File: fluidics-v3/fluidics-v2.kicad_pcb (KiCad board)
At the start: 4 copper layers, 85 x 95.5 mm, 82 parts, among them IC2 ADUM1250WSRZ-RL7, J1 PJ-063AH, J10 87832-0410, J11 0705430001, J12 87832-0410, J13 0705430001, J14 87832-0410, J15 0533980671, J16 0705430001, J17 0533980671, J18 87832-0410, J19 0705430001, J2 B6B-ZR-SM4-TF, J20 0533980671, J21 87832-0410, J22 0705430001, J24 0705430001, J25 87832-0410, J3 A-DS_15_A_KG-T4S, J4 B6B-ZR-SM4-TF, J5 Screw_Terminal_01x06, U1 TPL7407LDR, U11 MAX3221, U12 CD4050BDR, U13 TC7PZ17FU, U2 Teensy4.1, U3 AP7366EA-33W5-7, U4 D24V10FX, U6 LTC4311CSC6-TRPBF

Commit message: v3: mounting holes M2->M3, relink C3/C4/C10, regen fab package
Mounting holes H2-H4: MountingHole_2.2mm_M2 -> 3.2mm_M3 (PCB + schematic,
parity clean). Note: still 3 holes, no H1 (the original board had 4x M3).

Fix bulk-cap schematic links. C3/C4/C10 had no (path) link to their
symbols and lacked the library prefix in their footprint id, so "Update
PCB from Schematic" deleted and re-added them (losing routing). Relinked:
- C3  Capacitor_Tantalum_SMD:CP_EIA-7343-20_Kemet-V -> /cbfc97bd
- C4  Capacitor_SMD:C_1206_3216Metric              -> /5064b71f
- C10 Capacitor_SMD:C_1210_3225Metric              -> /25d2ffd2

Regenerated fabrication/v3 (gerbers, drill incl. new 3.2mm tool, gerber
zip, STEP, BOM, positions) to reflect the M3 holes.

DRC: 0 clearance/hole/short/isolated, 0 schematic-parity. Remaining are
pre-existing: 24 malformed_courtyard on U2 (footprint geometry) and 6
unconnected (5 intentional U2 no-connects + 1 +5V stub).

Co-Authored-By: Claude Opus 4.8 (1M context) <noreply@anthropic.com>
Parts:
- C10: footprint C_1210_3225Metric -> Capacitor_SMD:C_1210_3225Metric
- C3: footprint CP_EIA-7343-20_Kemet-V -> Capacitor_Tantalum_SMD:CP_EIA-7343-20_Kemet-V
- C4: footprint C_1206_3216Metric -> Capacitor_SMD:C_1206_3216Metric
- H2, H3, H4: footprint MountingHole:MountingHole_2.2mm_M2_Pad_Via -> MountingHole:MountingHole_3.2mm_M3_Pad_Via
- moved H3 3.30 mm to (188.7, 111.7)
- moved H2 1.04 mm to (114.0, 38.6)
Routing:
- net /Selector Valves/SCL 5V: track 86.3 -> 86.0 mm, vias 2 -> 1

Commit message: v3: align mounting holes to shared X/Y + regen fab
Snap M3 mounting holes onto shared orthogonal lines for manufacturing:
- Left column H2, H4 -> X = 114 (H4 moved 115->114; H2 kept, since X=115
  overlaps C6 courtyard + the +24V zone)
- Bottom row  H4, H3 -> Y = 112 (H3 moved 111.697->112)

Refilled all 8 copper zones so the +24V/+5V planes carve correctly
around the relocated holes. Regenerated fabrication/v3 (gerbers, drill,
gerber zip, STEP, positions) to match.

DRC: 0 clearance/hole/courtyard/short/isolated, 0 schematic-parity.
Remaining pre-existing: 24 malformed_courtyard on U2, 6 unconnected
(5 intentional U2 no-connects + 1 +5V stub).

Co-Authored-By: Claude Opus 4.8 (1M context) <noreply@anthropic.com>
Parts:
- moved H4 1.00 mm to (114.0, 112.0)
- moved H3 0.30 mm to (188.7, 112.0)
- turned H2 to 90 degrees
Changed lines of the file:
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@@
 	(footprint "MountingHole:MountingHole_3.2mm_M3_Pad_Via"
 		(layer "F.Cu")
-		(at 114 38.631)
+		(at 114 38.631 90)
 		(descr "Mounting Hole 3.2mm, M3, generated by kicad-footprint-generator mountinghole.py")
 		(tags "mountinghole M3")
 		(property "Reference" "H2"
-			(at 0 -4.15 0)
+			(at 0 -4.15 90)
 			(layer "F.SilkS")
 			(effects
@@
 		)
 		(property "Value" "MountingHole_Pad"
-			(at 0 4.15 0)
+			(at 0 4.15 90)
 			(layer "F.Fab")
 			(effects
@@
 		)
 		(property "Datasheet" ""
-			(at 0 0 0)
+			(at 0 0 90)
 			(layer "F.Fab")
 			(hide yes)
@@
 		)
 		(property "Description" ""
-			(at 0 0 0)
+			(at 0 0 90)
 			(layer "F.Fab")
 			(hide yes)
@@
 		)
 		(property "KiLib_Generator" "mounting_hardware/mounting_hole"
-			(at 0 0 0)
+			(at 0 0 90)
 			(layer "F.SilkS")
 			(hide yes)
@@
 		)
 		(fp_text user "${REFERENCE}"
-			(at 0 0 0)
+			(at 0 0 90)
 			(layer "F.Fab")
 			(effects
@@
 		)
 		(pad "1" thru_hole circle
-			(at -2.4 0)
+			(at -2.4 0 90)
 			(size 0.8 0.8)
 			(drill 0.5)
@@
 		)
 		(pad "1" thru_hole circle
-			(at -1.697056 -1.697056)
+			(at -1.697056 -1.697056 90)
 			(size 0.8 0.8)
 			(drill 0.5)
@@
 		)
 		(pad "1" thru_hole circle
-			(at -1.697056 1.697056)
+			(at -1.697056 1.697056 90)
 			(size 0.8 0.8)
 			(drill 0.5)
@@
 		)
 		(pad "1" thru_hole circle
-			(at 0 -2.4)
+			(at 0 -2.4 90)
 			(size 0.8 0.8)
 			(drill 0.5)
@@
 		)
 		(pad "1" thru_hole circle
-			(at 0 0)
+			(at 0 0 90)
 			(size 6.4 6.4)
 			(drill 3.2)
@@
 		)
 		(pad "1" thru_hole circle
-			(at 0 2.4)
+			(at 0 2.4 90)
 			(size 0.8 0.8)
 			(drill 0.5)
@@
 		)
 		(pad "1" thru_hole circle
-			(at 1.697056 -1.697056)
+			(at 1.697056 -1.697056 90)
 			(size 0.8 0.8)
 			(drill 0.5)
@@
 		)
 		(pad "1" thru_hole circle
-			(at 1.697056 1.697056)
+			(at 1.697056 1.697056 90)
 			(size 0.8 0.8)
 			(drill 0.5)
@@
 		)
 		(pad "1" thru_hole circle
-			(at 2.4 0)
+			(at 2.4 0 90)
 			(size 0.8 0.8)
 			(drill 0.5)
@@
 	(footprint "MountingHole:MountingHole_3.2mm_M3_Pad_Via"
 		(layer "F.Cu")
-		(at 115 112)
+		(at 114 112)
 		(descr "Mounting Hole 3.2mm, M3, generated by kicad-footprint-generator mountinghole.py")
 		(tags "mountinghole M3")
@@
 	(footprint "MountingHole:MountingHole_3.2mm_M3_Pad_Via"
 		(layer "F.Cu")
-		(at 188.697056 111.697056)
+		(at 188.697056 112)
 		(descr "Mounting Hole 3.2mm, M3, generated by kicad-footprint-generator mountinghole.py")
 		(tags "mountinghole M3")

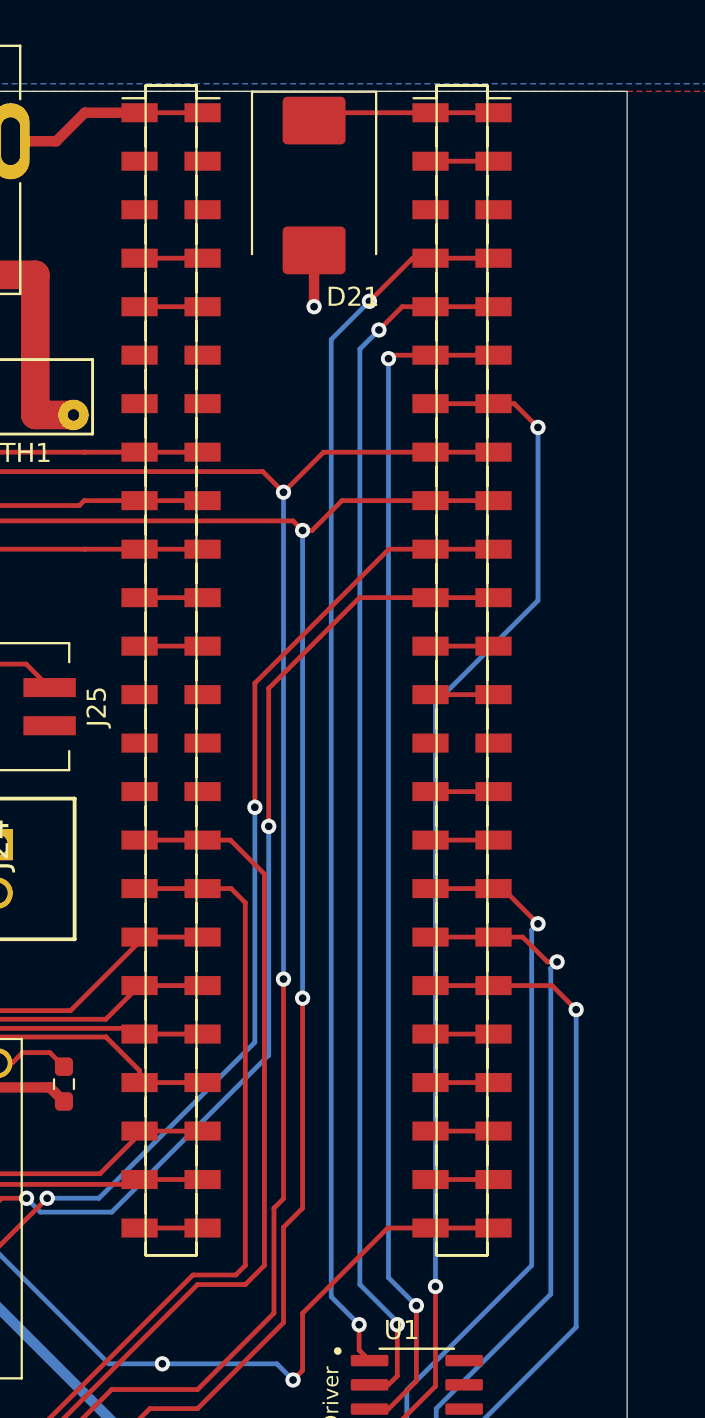
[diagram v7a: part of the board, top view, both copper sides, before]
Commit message: Split Teensy U2 into module + two 1x24 SMT sockets
U2 was one part standing in for three physical items: the Teensy 4.1 module
and the two 24-pin SMT socket strips it plugs into. The sockets existed only
as 3D models -- no refdes, no BOM line, no CPL entry -- so an assembler had
no way to order or place them.

New footprint teensy4.1:PinSocket_1x24_P2.54mm_Vertical_SMD_DualLand: 48 pads,
pin numbers 1-24 doubled, coordinates lifted verbatim from U2's lands. Every
pin has a land on both sides (the union of the Harwin M20-786 pin1-left and
pin1-right tail patterns), so strips fit in either orientation and a row may
be made up from shorter pieces. One footprint serves both sockets -- J7 is J6
rotated 180 degrees, which is why J7 pin n lands on old U2 pin n+24.

Schematic: J6/J7 (Conn_01x24) carry the 48 nets via labels on the root sheet;
GND power symbols on J6.1/J7.10/J7.23; no-connect flags on J6.2/J6.3/J6.15/
J7.22. U2 keeps its symbol and BOM line but is marked exclude-from-board.
Seven nets that had no root-sheet name were named to make the join explicit:
/Bubble Sensors/{2B,2A,1B,1A,Calib 2,Calib 1} 3.3V -> BUB_*, Net-(D21-K) -> VIN.

PCB: J6 at (170.61, 51.33) rot 0, J7 at (185.85, 51.33) rot 180 -- all 96 pads
sit exactly on the coordinates U2's lands occupied, so no copper moved. U2's
footprint removed. Module body added back as documentation: 61.0 x 17.78 mm
outline plus "U2 Teensy 4.1" on F.Fab, "U2 TEENSY 4.1" on F.Silkscreen in the
pad-free channel between the rows (no outline on silk -- the body edges cross
the socket lands, which is what generated the old silk_over_copper count).

Verified: 44/44 socket pins on the same net as their former U2 pin, 4/4
intended no-connects, 0 nets lost or created. DRC unconnected 6 (unchanged
baseline: 5 GPIO_8/9+SPI no-connects, 1 pre-existing +5V stub gap), schematic
parity 0, 0 electrical violations. Cosmetic violations 209 -> 85 (U2's
footprint took 24 malformed courtyards and ~96 silk_over_copper with it).
ERC introd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
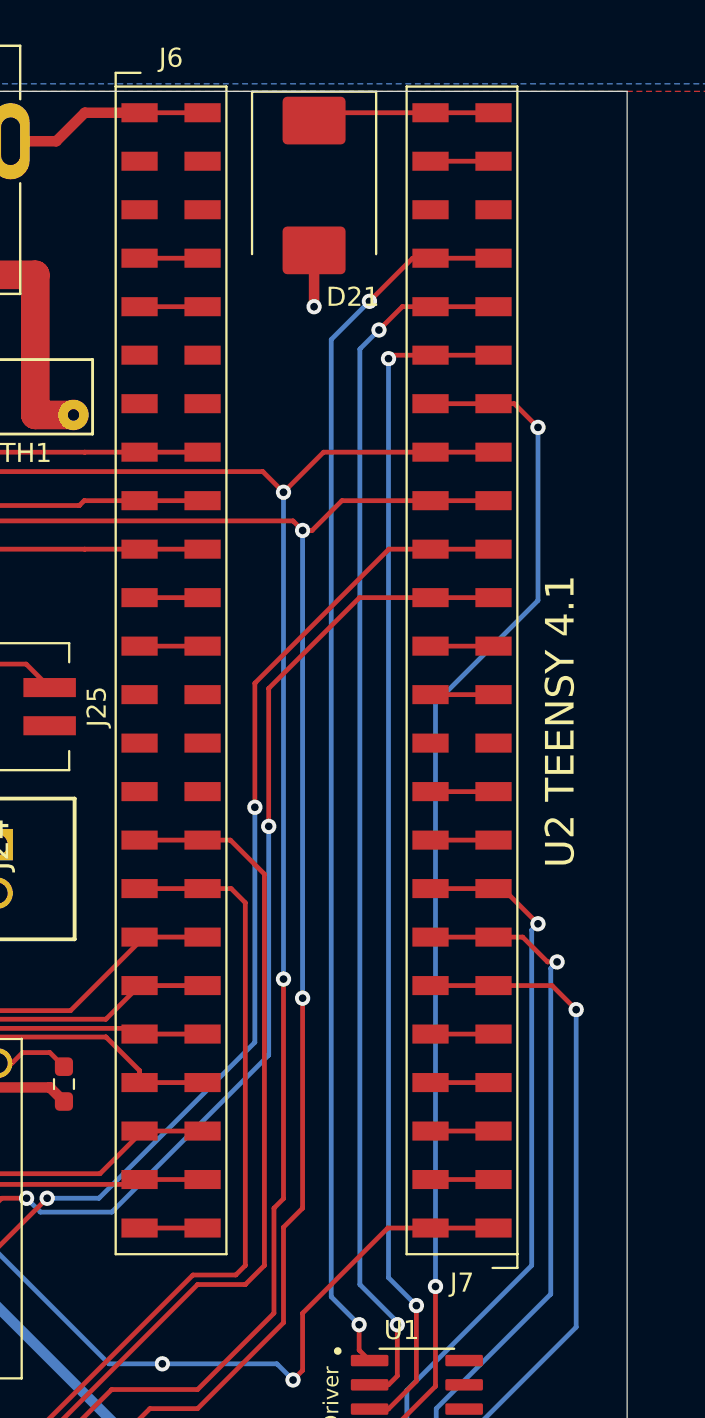
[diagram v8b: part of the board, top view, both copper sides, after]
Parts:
- removed U2: Teensy4.1, teensy4.1:Teensy 4.1
- added J6: Socket_1x24_2.54mm_SMT, teensy4.1:PinSocket_1x24_P2.54mm_Vertical_SMD_DualLand, F.Cu at (170.6, 51.3)
- added J7: Socket_1x24_2.54mm_SMT, teensy4.1:PinSocket_1x24_P2.54mm_Vertical_SMD_DualLand, F.Cu at (185.8, 51.3)
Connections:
- D21 pad 1: Net-(D21-K) -> /VIN
- U12 pad 10: /Bubble Sensors/2B 3.3V -> /BUB_2B
- U12 pad 2: /Bubble Sensors/1A 3.3V -> /BUB_1A
- U12 pad 4: /Bubble Sensors/1B 3.3V -> /BUB_1B
- U12 pad 6: /Bubble Sensors/2A 3.3V -> /BUB_2A
- U13 pad 1: /Bubble Sensors/Calib 1 3.3V -> /BUB_CALIB1
- U13 pad 3: /Bubble Sensors/Calib 2 3.3V -> /BUB_CALIB2
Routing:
- net /Bubble Sensors/2B 3.3V: track 47.0 -> 0.00 mm
- net /BUB_2B: track 0.00 -> 47.0 mm
- net /Bubble Sensors/Calib 2 3.3V: track 40.0 -> 0.00 mm
- net /BUB_CALIB2: track 0.00 -> 40.0 mm
- net /Bubble Sensors/Calib 1 3.3V: track 38.8 -> 0.00 mm
- net /BUB_CALIB1: track 0.00 -> 38.8 mm
- net /Bubble Sensors/2A 3.3V: track 37.8 -> 0.00 mm
- net /BUB_2A: track 0.00 -> 37.8 mm
- net /Bubble Sensors/1B 3.3V: track 35.4 -> 0.00 mm
- net /BUB_1B: track 0.00 -> 35.4 mm
- net /Bubble Sensors/1A 3.3V: track 33.9 -> 0.00 mm
- net /BUB_1A: track 0.00 -> 33.9 mm
- net Net-(D21-K): track 9.57 -> 0.00 mm
- net /VIN: track 0.00 -> 9.57 mm
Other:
- board text added: "U2 TEENSY 4.1"
- board text added: "U2 Teensy 4.1"
